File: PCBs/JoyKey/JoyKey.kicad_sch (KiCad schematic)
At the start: 6 parts, among them J1 OLED_DISPLAY, J3 Testpad wire hole1, U2 LSM6DSL, U3 XIAO-RP2040-DIP

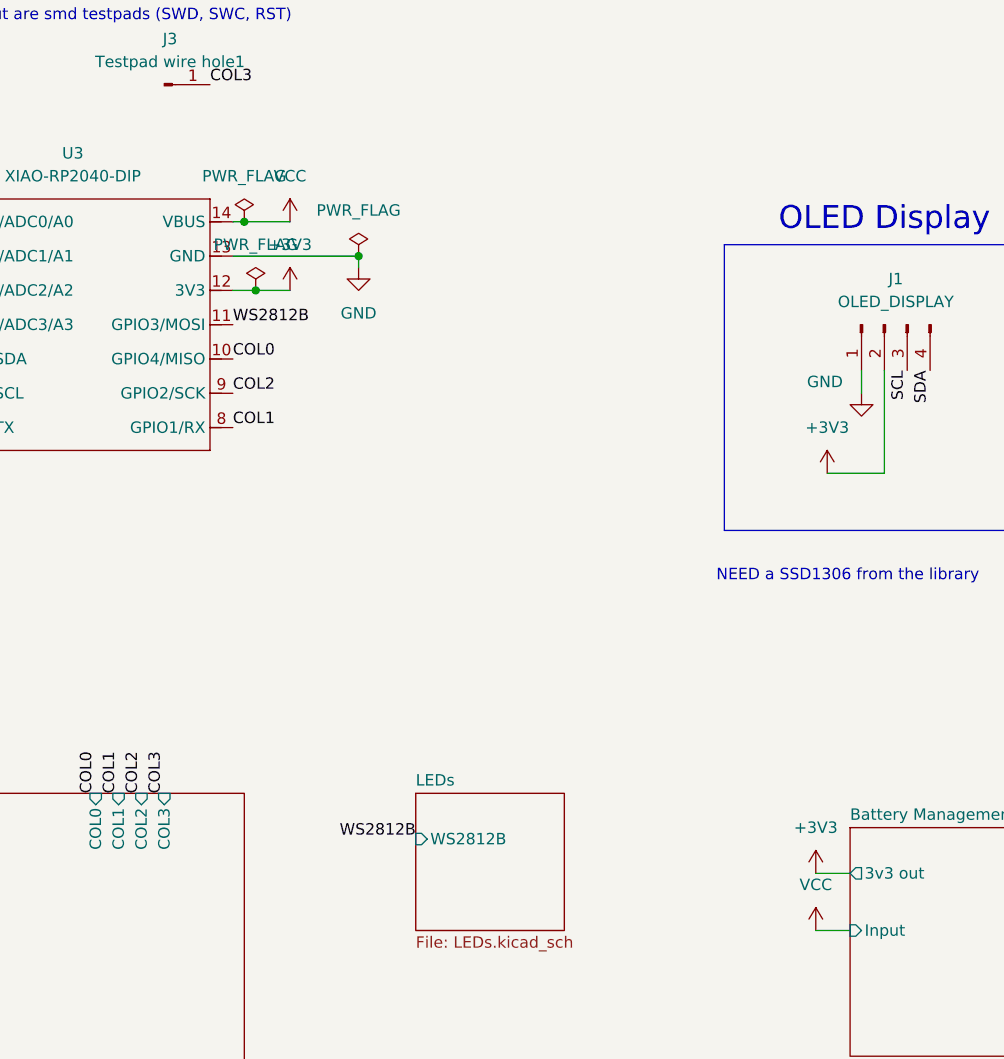
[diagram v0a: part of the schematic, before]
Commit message: Updated Battery Management to Adafruit Feather system
I wanted to use a proven design that was low cost, and this seemed the best option. Only modification is removing the 5v input to the 3.3v regulator so that I don't have two regulators fighting
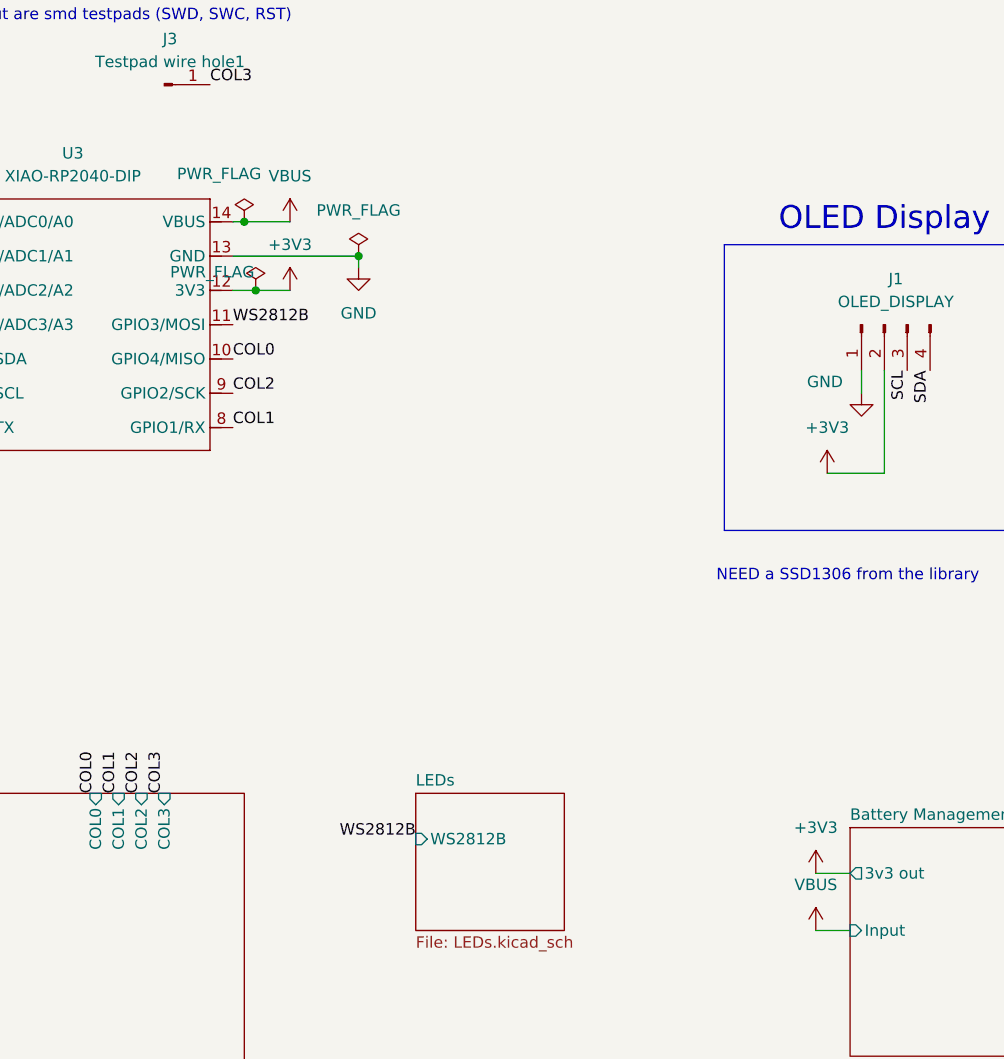
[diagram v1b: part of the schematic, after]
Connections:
- net VCC renamed VBUS
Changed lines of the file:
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@@
 		(on_board yes)
 		(dnp no)
-		(fields_autoplaced yes)
 		(property "Reference" "#FLG02"
 			(at 139.7 38.735 0)
@@
 		)
 		(property "Value" "PWR_FLAG"
-			(at 139.7 35.56 0)
+			(at 136.906 35.306 0)
 			(effects
 				(font
@@
 	)
 	(symbol
-		(lib_id "power:VCC")
+		(lib_id "power:VBUS")
 		(at 144.78 40.64 0)
 		(unit 1)
@@
 			)
 		)
-		(property "Value" "VCC"
+		(property "Value" "VBUS"
 			(at 144.78 35.56 0)
 			(effects
@@
 			)
 		)
-		(property "Description" "Power symbol creates a global label with name \"VCC\""
+		(property "Description" "Power symbol creates a global label with name \"VBUS\""
 			(at 144.78 40.64 0)
 			(effects
@@
 		(on_board yes)
 		(dnp no)
-		(fields_autoplaced yes)
 		(property "Reference" "#FLG03"
 			(at 140.97 46.355 0)
@@
 		)
 		(property "Value" "PWR_FLAG"
-			(at 140.97 43.18 0)
+			(at 136.144 46.228 0)
 			(effects
 				(font
@@
 	)
 	(symbol
-		(lib_id "power:VCC")
+		(lib_id "power:VBUS")
 		(at 203.2 119.38 0)
 		(unit 1)
@@
 		(dnp no)
 		(fields_autoplaced yes)
-		(property "Reference" "#PWR018"
+		(property "Reference" "#PWR18"
 			(at 203.2 123.19 0)
 			(effects
@@
 			)
 		)
-		(property "Value" "VCC"
+		(property "Value" "VBUS"
 			(at 203.2 114.3 0)
 			(effects
@@
 			)
 		)
-		(property "Description" "Power symbol creates a global label with name \"VCC\""
+		(property "Description" "Power symbol creates a global label with name \"VBUS\""
 			(at 203.2 119.38 0)
 			(effects
@@
 			(project "JoyKey"
 				(path "/7995ec7a-c14b-437e-b354-3eb74052b7cb"
-					(reference "#PWR018")
-					(unit 1)
-				)
+					(reference "#PWR18")
+					(unit 1)
+				)

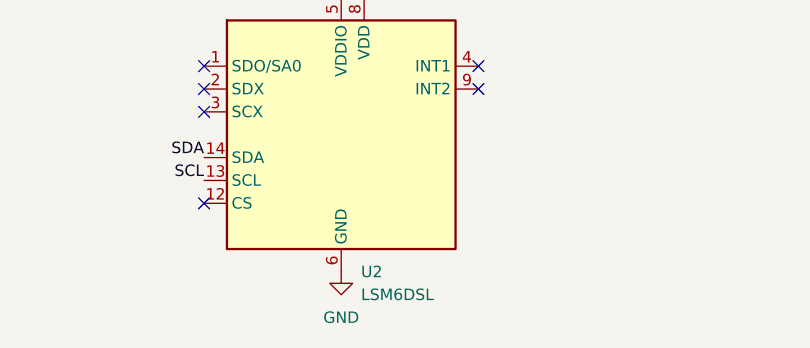
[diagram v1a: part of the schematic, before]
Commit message: Switched out accel+gyro unit
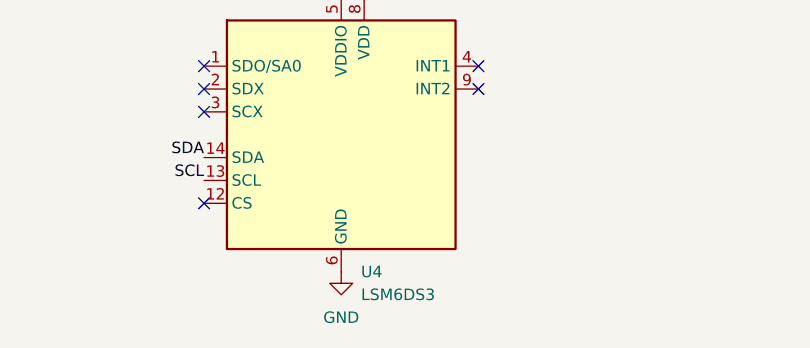
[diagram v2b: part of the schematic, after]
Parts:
- removed U2: LSM6DSL, Package_LGA:LGA-14_3x2.5mm_P0.5mm_LayoutBorder3x4y, symbol Sensor_Motion:LSM6DSL
- added U4: LSM6DS3, Package_LGA:LGA-14_3x2.5mm_P0.5mm_LayoutBorder3x4y, symbol Sensor_Motion:LSM6DS3
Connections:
- net +3V3: now also U4.5 (VDDIO), U4.8 (VDD)
- net GND: now also U4.6 (GND), U4.7 (GND)
- net SCL: now also U4.13 (SCL)
- net SDA: now also U4.14 (SDA)
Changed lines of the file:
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@@
+	)
+	(symbol
+		(lib_id "Sensor_Motion:LSM6DS3")
+		(at 135.89 161.29 0)
+		(unit 1)
+		(exclude_from_sim no)
+		(in_bom yes)
+		(on_board yes)
+		(dnp no)
+		(fields_autoplaced yes)
+		(property "Reference" "U4"
+			(at 138.0841 176.53 0)
+			(effects
+				(font
+					(size 1.27 1.27)
+				)
+				(justify left)
+			)
+		)
+		(property "Value" "LSM6DS3"
+			(at 138.0841 179.07 0)
+			(effects
+				(font
+					(size 1.27 1.27)
+				)
+				(justify left)
+			)
+		)
+		(property "Footprint" "Package_LGA:LGA-14_3x2.5mm_P0.5mm_LayoutBorder3x4y"
+			(at 125.73 179.07 0)
+			(effects
+				(font
+					(size 1.27 1.27)
+				)
+				(justify left)
+				(hide yes)
+			)
+		)
+		(property "Datasheet" "https://www.st.com/resource/en/datasheet/lsm6ds3tr-c.pdf"
+			(at 138.43 177.8 0)
+			(effects
+				(font
+					(size 1.27 1.27)
+				)
+				(hide yes)
+			)
+		)
+		(property "Description" "I2C/SPI, iNEMO inertial module: always-on 3D accelerometer and 3D gyroscope"
+			(at 135.89 161.29 0)
+			(effects
+				(font
+					(size 1.27 1.27)
+				)
+				(hide yes)
+			)
+		)
+		(pin "14"
+		)
+		(pin "3"
+		)
+		(pin "4"
+		)
+		(pin "8"
+		)
+		(pin "9"
+		)
+		(pin "5"
+		)
+		(pin "6"
+		)
+		(pin "7"
+		)
+		(pin "13"
+		)
+		(pin "2"
+		)
+		(pin "11"
+		)
+		(pin "12"
+		)
+		(pin "10"
+		)
+		(pin "1"
+		)
+		(instances
+			(project ""
+				(path "/7995ec7a-c14b-437e-b354-3eb74052b7cb"
+					(reference "U4")
+					(unit 1)
+				)
+			)
+		)
 	)
 	(symbol
@@
 					(unit 1)
 				)
-			)
-		)
-	)
-	(symbol
-		(lib_id "Sensor_Motion:LSM6DSL")
-		(at 135.89 161.29 0)
-		(unit 1)
-		(exclude_from_sim no)
-		(in_bom yes)
-		(on_board yes)
-		(dnp no)
-		(fields_autoplaced yes)
-		(property "Reference" "U2"
-			(at 138.0841 176.53 0)
-			(effects
-				(font
-					(size 1.27 1.27)
-				)
-				(justify left)
-			)
-		)
-		(property "Value" "LSM6DSL"
-			(at 138.0841 179.07 0)
-			(effects
-				(font
-					(size 1.27 1.27)
-				)
-				(justify left)
-			)
-		)
-		(property "Footprint" "Package_LGA:LGA-14_3x2.5mm_P0.5mm_LayoutBorder3x4y"
-			(at 125.73 179.07 0)
-			(effects
-				(font
-					(size 1.27 1.27)
-				)
-				(justify left)
-				(hide yes)
-			)
-		)
-		(property "Datasheet" "https://www.st.com/resource/en/datasheet/lsm6dsl.pdf"
-			(at 138.43 177.8 0)
-			(effects
-				(font
-					(size 1.27 1.27)
-				)
-				(hide yes)
-			)
-		)
-		(property "Description" "I2C/SPI, iNEMO inertial module: always-on 3D accelerometer and 3D gyroscope, 1.71V to 3.6V VCC"
-			(at 135.89 161.29 0)
-			(effects
-				(font
-					(size 1.27 1.27)
-				)
-				(hide yes)
-			)
-		)
-		(pin "6"
-		)
-		(pin "7"
-		)
-		(pin "8"
-		)
-		(pin "9"
-		)
-		(pin "5"
-		)
-		(pin "10"
-		)
-		(pin "2"
-		)
-		(pin "14"
-		)
-		(pin "13"
-		)
-		(pin "4"
-		)
-		(pin "3"
-		)
-		(pin "1"
-		)
-		(pin "11"
-		)
-		(pin "12"
-		)
-		(instances
-			(project ""
-				(path "/7995ec7a-c14b-437e-b354-3eb74052b7cb"
-					(reference "U2")
-					(unit 1)
-				)

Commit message: Changed footprint for Gyro to avoid copper clearance issues
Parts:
- U4: footprint Package_LGA:LGA-14_3x2.5mm_P0.5mm_LayoutBorder3x4y -> custom_Interface_HID:LGA-14_3x2.5mm_P0.5mm_LayoutBorder3x4y_COSTSAVERPADs
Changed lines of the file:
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@@
 			)
 		)
-		(property "Footprint" "Package_LGA:LGA-14_3x2.5mm_P0.5mm_LayoutBorder3x4y"
+		(property "Footprint" "custom_Interface_HID:LGA-14_3x2.5mm_P0.5mm_LayoutBorder3x4y_COSTSAVERPADs"
 			(at 125.73 179.07 0)
 			(effects
